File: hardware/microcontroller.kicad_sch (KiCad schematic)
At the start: 17 parts, among them SW1 SW_Push

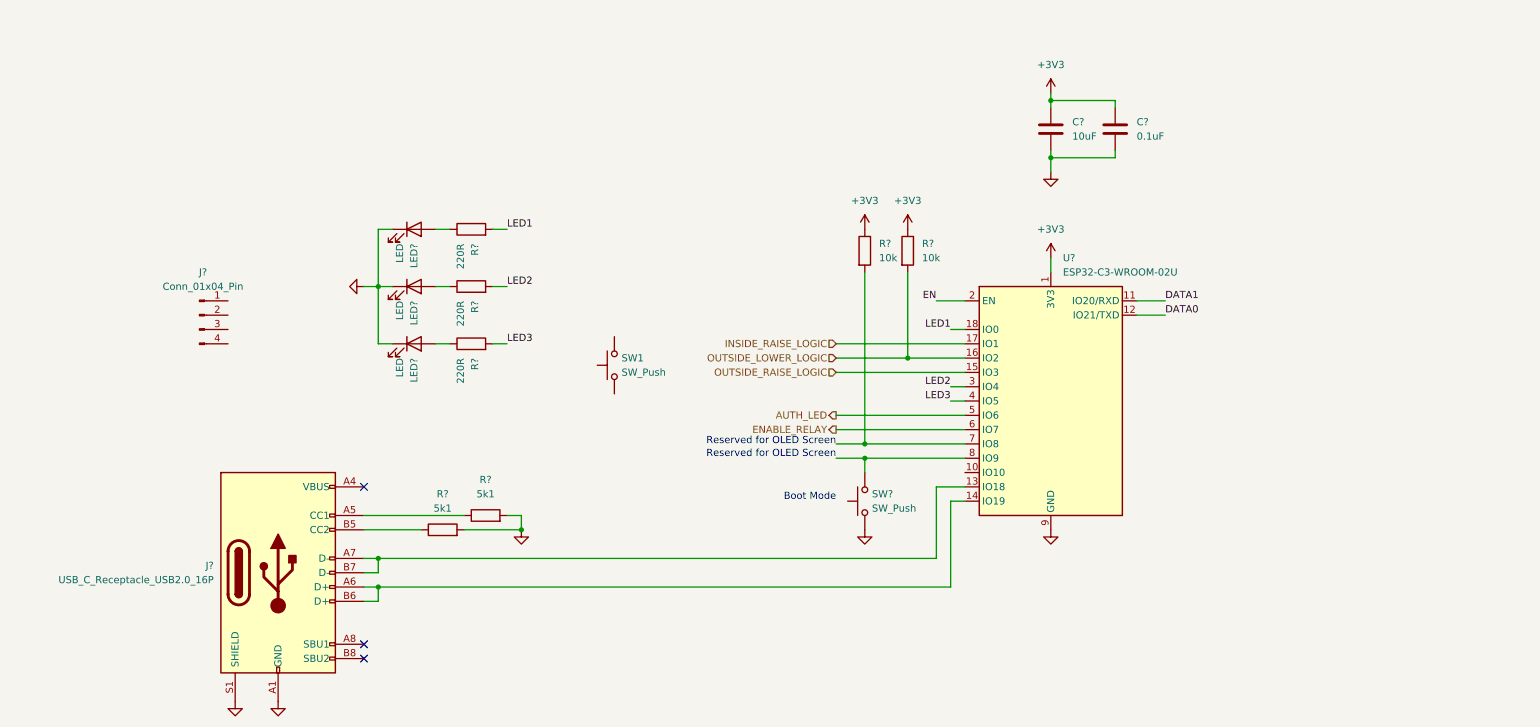
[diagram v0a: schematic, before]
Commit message: swapped DC-DCs, upgraded to S3
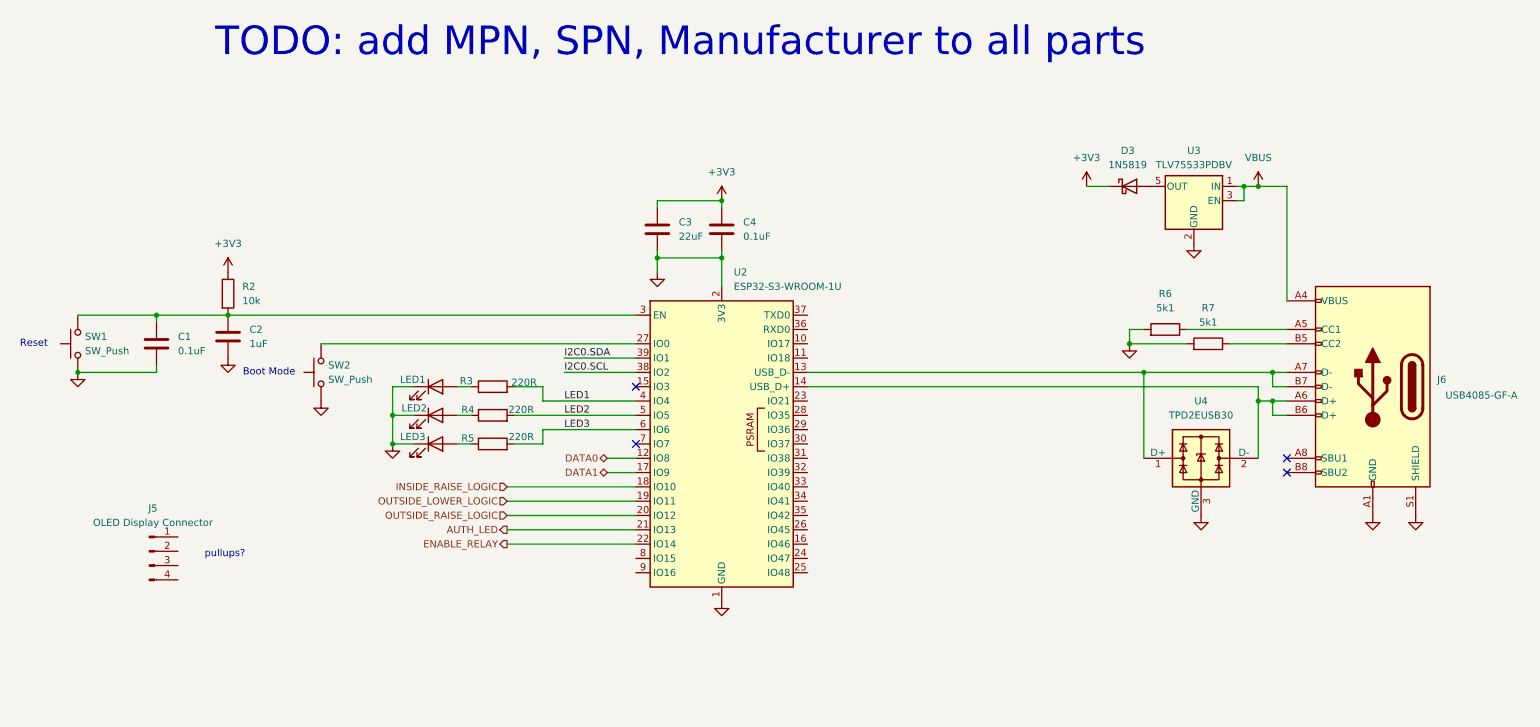
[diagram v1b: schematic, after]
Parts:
- removed C?: 0.1uF, Capacitor_SMD:C_0603_1608Metric_Pad1.08x0.95mm_HandSolder, symbol Device:C
- removed C?: 10uF, Capacitor_SMD:C_1210_3225Metric_Pad1.33x2.70mm_HandSolder, symbol Device:C
- removed R? (x2): 10k, Resistor_SMD:R_0402_1005Metric, symbol Device:R
- removed U?: ESP32-C3-WROOM-02U, RF_Module:ESP32-C3-WROOM-02U, symbol RF_Module:ESP32-C3-WROOM-02U
- added C1, C4: 0.1uF, Capacitor_SMD:C_0402_1005Metric_Pad0.74x0.62mm_HandSolder, symbol Device:C
- added C2: 1uF, Capacitor_SMD:C_0402_1005Metric_Pad0.74x0.62mm_HandSolder, symbol Device:C
- added C3: 22uF, Capacitor_SMD:C_0805_2012Metric_Pad1.18x1.45mm_HandSolder, symbol Device:C
- added D3: 1N5819, Diode_THT:D_DO-41_SOD81_P10.16mm_Horizontal, symbol Diode:1N5819
- added R2: 10k, Resistor_SMD:R_0402_1005Metric, symbol Device:R
- added U2: ESP32-S3-WROOM-1U, RF_Module:ESP32-S3-WROOM-1U, symbol RF_Module:ESP32-S3-WROOM-1
- added U3: TLV75533PDBV, Package_TO_SOT_SMD:SOT-23-5_HandSoldering, symbol Regulator_Linear:TLV75533PDBV
- added U4: TPD2EUSB30, Package_TO_SOT_SMD:Texas_DRT-3, symbol Power_Protection:TPD2EUSB30
- J5: renamed from J?; value Conn_01x04_Pin -> OLED Display Connector
- J6: renamed from J?; MPN (none) -> USB4085-GF-A; Manufacturer (none) -> GCT
- gave numbers to parts that had none: 9
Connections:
- net +3V3: now also C3.1, C4.1, D3.1 (K), R2.1
- net AUTH_LED: now also U2.21 (IO13)
- net DATA0: now also U2.12 (IO8)
- net DATA1: now also U2.17 (IO9)
- net ENABLE_RELAY: now also U2.22 (IO14)
- net GND: now also SW1.1, C1.2, C2.2, C3.2, C4.2, U2.1 (GND), U2.2 (3V3), U2.40 (GND), U2.41 (GND), U3.2 (GND), U4.3 (GND)
- net INSIDE_RAISE_LOGIC: now also U2.18 (IO10)
- net LED1: now also U2.4 (IO4)
- net LED2: now also U2.5 (IO5)
- net LED3: now also U2.6 (IO6)
- net OUTSIDE_LOWER_LOGIC: now also U2.19 (IO11)
- net OUTSIDE_RAISE_LOGIC: now also U2.20 (IO12)
- net VBUS: now reaches J6.A4 (VBUS), J6.A9 (VBUS), J6.B4 (VBUS), J6.B9 (VBUS)
- net VBUS: now also U3.1 (IN), U3.3 (EN)
- net at J6.A6 (D+), J6.B6 (D+): now also U2.14 (USB_D+), U4.2 (D-)
- net at J6.A7 (D-), J6.B7 (D-): now also U2.13 (USB_D-), U4.1 (D+)
- net at SW2.2: now also U2.27 (IO0)
- net at SW1.2: now also C1.1, C2.1, R2.2, U2.3 (EN)
- new net: D3.2 (A), U3.5 (OUT)
- new net I2C0.SCL: U2.38 (IO2)
- new net I2C0.SDA: U2.39 (IO1)
- no-connect marks 3 -> 4
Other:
- note added: "Reset"
- note added: "TODO: add MPN, SPN, Manufacturer to all parts"
- note added: "pullups?"
- note removed: "Reserved for OLED Screen"
- moved on the sheet: J5, J6, LED1, LED2, LED3, R3, R4, R5, R6, R7, SW1, SW2

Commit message: schematic WIP
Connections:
- net BUZZER_INT: now reaches U2.8 (IO15)
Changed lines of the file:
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@@
+	)
+	(junction
+		(at 107.95 101.6)
+		(diameter 0)
+		(color 0 0 0 0)
 	)
 	(junction
@@
 	(wire
 		(pts
+			(xy 107.95 104.14) (xy 107.95 101.6)
+		)
+		(stroke
+			(width 0)
+			(type default)
+		)
+	)
+	(wire
+		(pts
 			(xy 154.94 91.44) (xy 234.95 91.44)
 		)
@@
 	(wire
 		(pts
+			(xy 101.6 104.14) (xy 107.95 104.14)
+		)
+		(stroke
+			(width 0)
+			(type default)
+		)
+	)
+	(wire
+		(pts
 			(xy 237.49 93.98) (xy 237.49 96.52)
 		)
@@
 		(pts
 			(xy 240.03 88.9) (xy 237.49 88.9)
+		)
+		(stroke
+			(width 0)
+			(type default)
+		)
+	)
+	(wire
+		(pts
+			(xy 101.6 121.92) (xy 124.46 121.92)
 		)
 		(stroke
@@
 		(effects
 			(font
+				(size 1.27 1.27)
+			)
+			(justify right)
+		)
+	)
+	(hierarchical_label "BUZZER_INT"
+		(shape output)
+		(at 101.6 121.92 180)
+		(effects
+			(font
+				(size 1.27 1.27)
+			)
+			(justify right)
+		)
+	)
+	(hierarchical_label "LED3"
+		(shape output)
+		(at 101.6 104.14 180)
+		(effects
+			(font

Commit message: wip
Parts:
- J5: value OLED Display Connector -> 5-146274-4; DigiKey (none) -> A122867-ND; MPN (none) -> 5-146274-4; Manufacturer (none) -> TE
- SW1, SW2: value SW_Push -> TL3305BF260QG; footprint (none) -> Button_Switch_SMD:SW_SPST_TL3305B; DigiKey (none) -> EG5354CT-ND; MPN (none) -> TL3305BF260QG; Manufacturer (none) -> E-Switch
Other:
- note added: "GPIO header?"
- note added: "OLED Screen Header"
- moved on the sheet: SW1
